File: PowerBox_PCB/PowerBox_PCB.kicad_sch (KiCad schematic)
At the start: 0 parts

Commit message: Added Powersupplys
Added the TPS54620 as powersupplys and built circuit for it.
Added A LDO 5v 3A DC-DC VREG for the battery charger
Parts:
- added R17: 10kΩ, Resistor_SMD:R_0805_2012Metric_Pad1.20x1.40mm_HandSolder, symbol Custom_Symbols:10kRes
- added U10: (no value), Package_TO_SOT_SMD:TO-252-3_TabPin2, symbol Batt_Charger:LM1084RS-5.0
- added U9: (no value), Package_TO_SOT_SMD:SOT-23, symbol Custom_Symbols:2N7002
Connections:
- new net GND: R17.2, U10.1 (GND), U9.2 (S)
- new net Ideal_Diode/VIN_IDEAL: R17.1, U9.1 (G)
- new net TPS54620_Buck1/EN_BUCK: U9.3 (D)
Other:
- added sheet Ideal_Diode (Ideal_Diode.kicad_sch)
- added sheet Ideal_Diode1 (Ideal_Diode.kicad_sch)
- added sheet TPS54620_Buck (TPS54620_Buck.kicad_sch)
- added sheet TPS54620_Buck1 (TPS54620_Buck.kicad_sch)

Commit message: Added USBPD & BMD & BATTCHARGER
Added USBPD & BMD & BATTCHARGER
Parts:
- removed U10: (no value), Package_TO_SOT_SMD:TO-252-3_TabPin2, symbol Batt_Charger:LM1084RS-5.0
- added B1: 2S Batt Pack, Custom_Footprints:2S Batt Pack, symbol Batt_Charger:BatteryPack
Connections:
- new net BMS/B+: B1.1 (B+)
- new net BMS/B-: B1.3 (B-)
- new net BMS/BM: B1.2 (BM)
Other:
- added sheet BMS (BMS.kicad_sch)
- added sheet Batt Charger (Batt Charger.kicad_sch)
- added sheet USBPD (USBPD.kicad_sch)

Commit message: Finished
Basically done
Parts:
- added SW1: SW_DPDT_x2, Custom_Footprints:SwitchPads, symbol BMS:SW_DPDT_x2
- added TP1, TP10, TP12, TP13, TP2, TP3, TP4, TP5, TP6, TP7, TP8, TP9: (no value), Custom_Footprints:PAD-2x2, symbol Custom_Symbols:Pad-2x2
- added TP14, TP15, TP16, TP17: (no value), Custom_Footprints:M3-Pad, symbol Custom_Symbols:M3-PAD
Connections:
- net GND: now also TP10.1 (PAD), TP14.1 (PAD), TP15.1 (PAD), TP16.1 (PAD), TP17.1 (PAD), TP2.1 (PAD), TP9.1 (PAD)
- net Ideal_Diode/VIN_IDEAL: now also TP13.1 (PAD)
- net Ideal_Diode/VOUT_IDEAL: now also TP6.1 (PAD), TP8.1 (PAD)
- net Ideal_Diode1/VIN_IDEAL: now also TP12.1 (PAD)
- net P+: now also SW1.5 (B), TP3.1 (PAD)
- net PM: now also TP4.1 (PAD)
- net VUSBPD: now also SW1.2 (B), TP1.1 (PAD)
- new net TPS54620_Buck1/VIN_BUCK: SW1.4 (A), TP5.1 (PAD)
- new net VUSBPDSWITCHED: SW1.1 (A), TP7.1 (PAD)

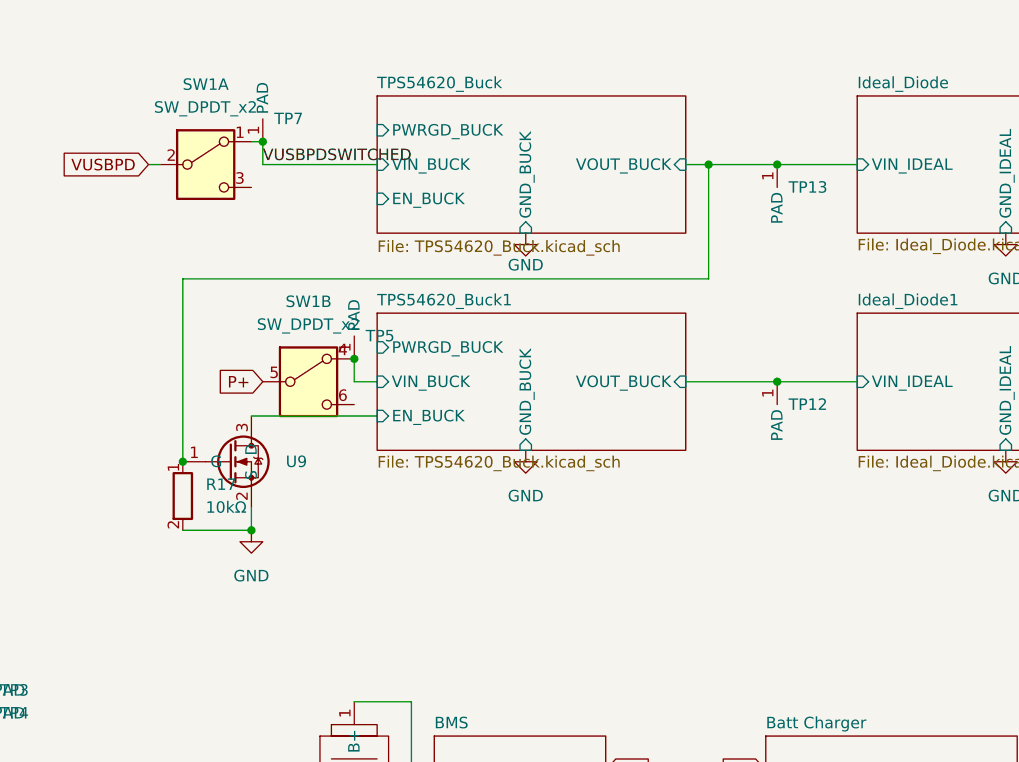
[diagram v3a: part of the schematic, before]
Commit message: add indicator lights
add indicator lights
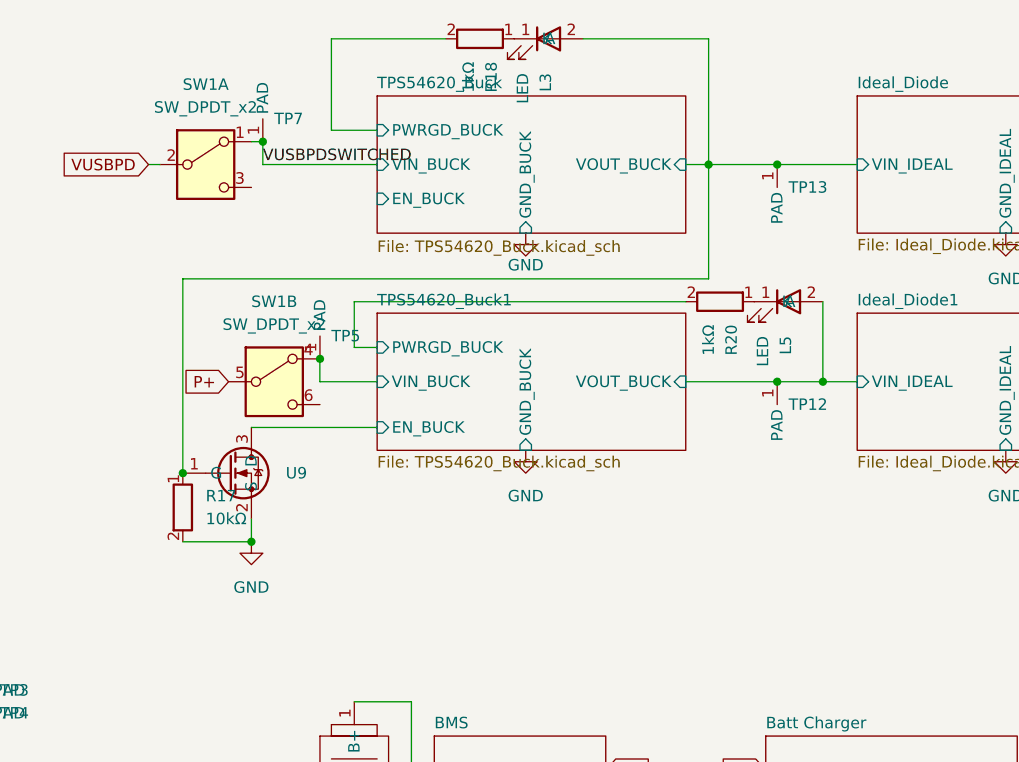
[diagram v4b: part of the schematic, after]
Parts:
- added L3, L5: LED, LED_SMD:LED_0805_2012Metric_Pad1.15x1.40mm_HandSolder, symbol Custom_Symbols:LED
- added R18, R20: 1kΩ, Resistor_SMD:R_0805_2012Metric_Pad1.20x1.40mm_HandSolder, symbol Custom_Symbols:1kRes
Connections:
- net Ideal_Diode/VIN_IDEAL: now also L3.2 (A)
- net Ideal_Diode1/VIN_IDEAL: now also L5.2 (A)
- net TPS54620_Buck/PWRGD_BUCK: now also R18.2
- net TPS54620_Buck1/PWRGD_BUCK: now also R20.2
- new net: L3.1 (K), R18.1
- new net: L5.1 (K), R20.1
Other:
- moved on the sheet: R17, SW1B, TP5, U9

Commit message: .
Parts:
- removed TP6, TP8: (no value), Custom_Footprints:PAD-2x2, symbol Custom_Symbols:Pad-2x2
- added TP18, TP19: (no value), Custom_Footprints:PAD-2x2-ThroughHole, symbol Custom_Symbols:Pad-2x2-ThroughHole
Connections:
- net Ideal_Diode/VOUT_IDEAL: now also TP18.1 (PAD), TP19.1 (PAD)

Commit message: fix bom
bom
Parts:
- U9: value (none) -> 2N7002
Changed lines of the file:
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@@
 			)
 		)
-		(property "Value" ""
+		(property "Value" "2N7002"
 			(at 127 81.28 0)
 			(show_name no)

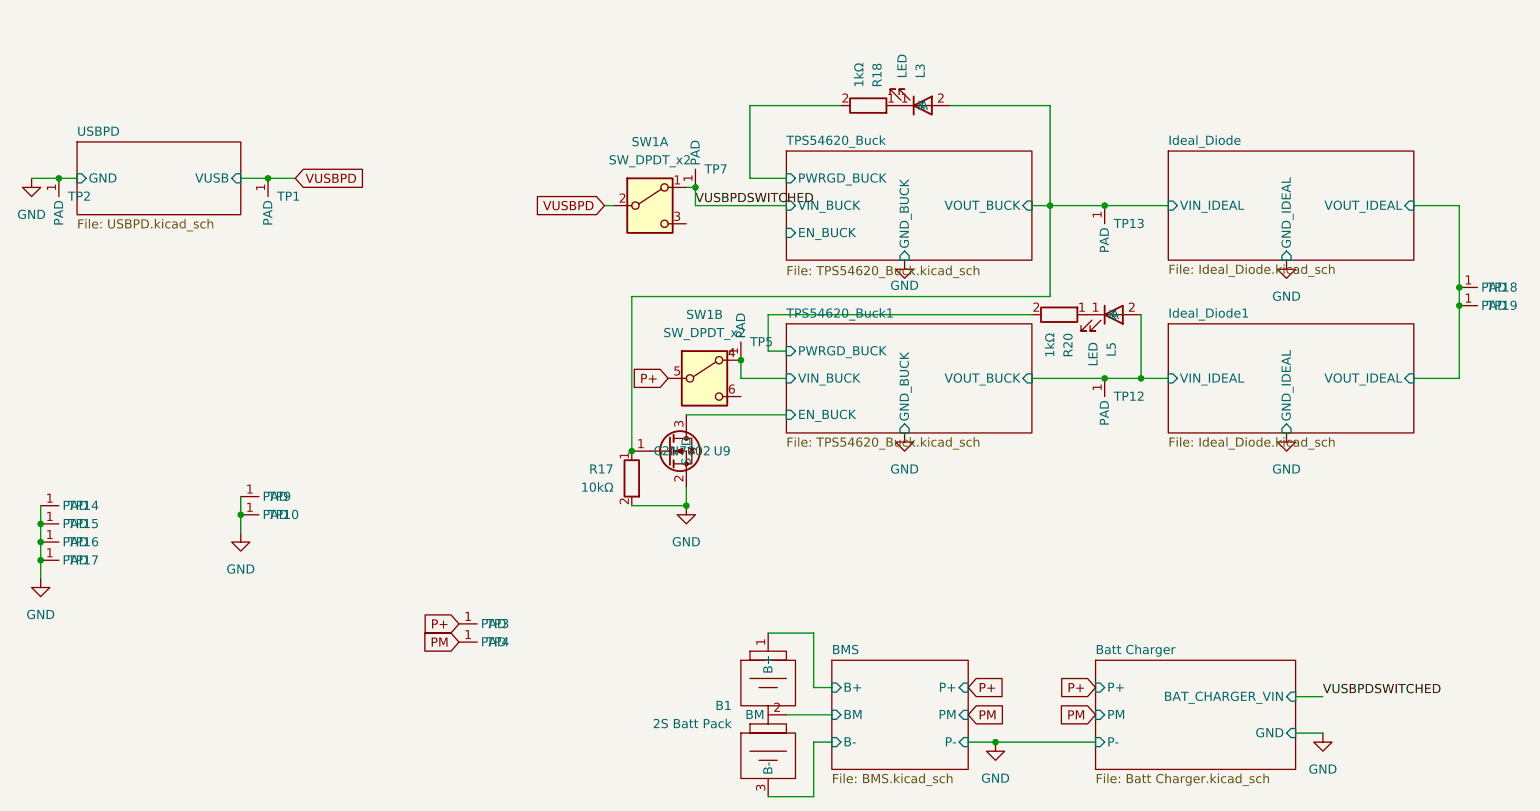
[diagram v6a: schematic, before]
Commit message: Changed HUSB238 to CH221K
HUSB238 Went out of stock so changed to CH221K
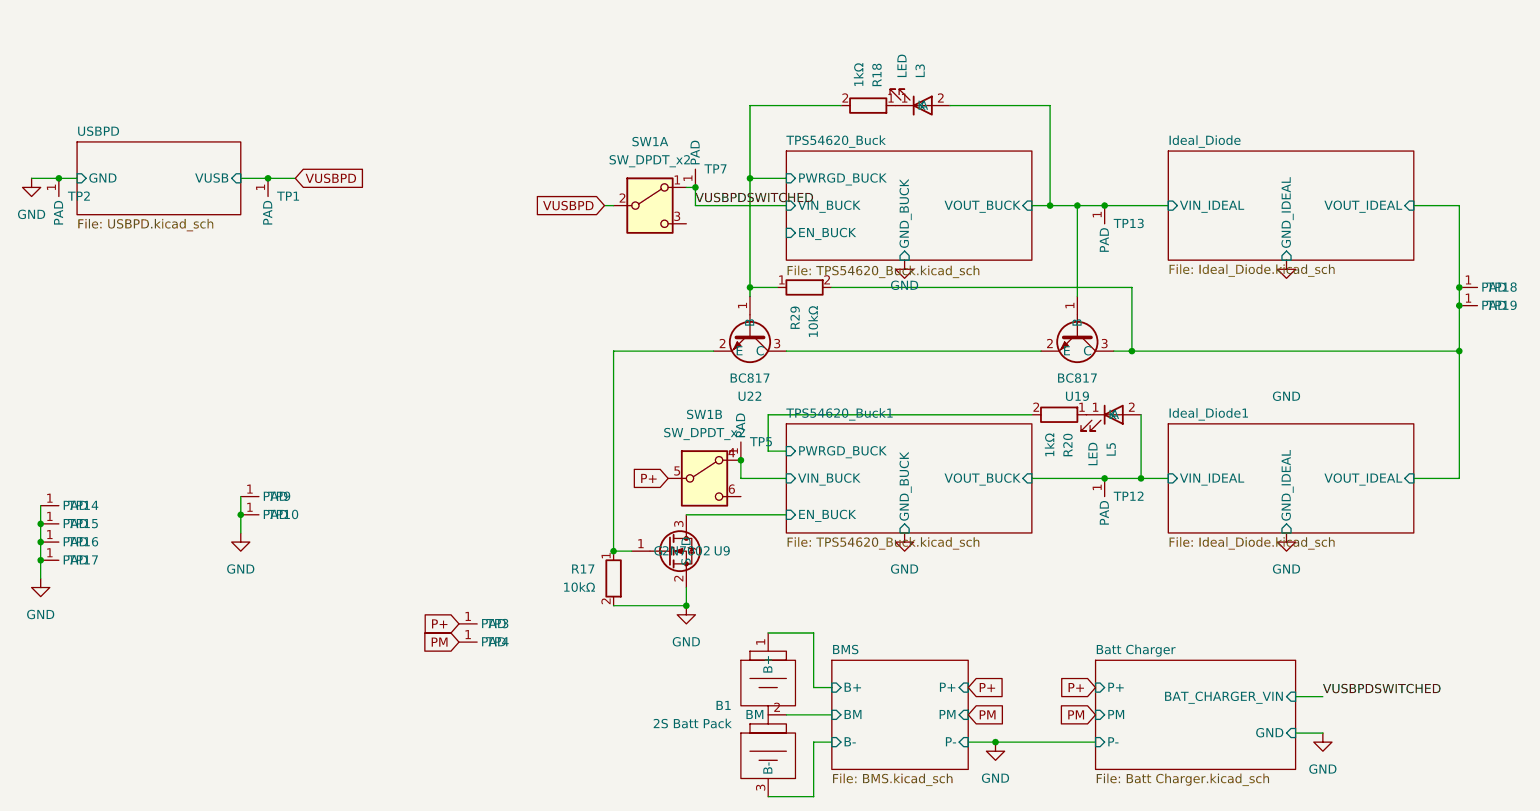
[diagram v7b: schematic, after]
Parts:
- added R29: 10kΩ, Resistor_SMD:R_0805_2012Metric_Pad1.20x1.40mm_HandSolder, symbol Custom_Symbols:10kRes
- added U19, U22: BC817, Package_TO_SOT_SMD:SOT-23, symbol Custom_Symbols:BC817-NPN
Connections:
- net Ideal_Diode/VIN_IDEAL: now also U19.1 (B); no longer R17.1, U9.1 (G)
- net Ideal_Diode/VOUT_IDEAL: now also R29.2, U19.3 (C)
- net TPS54620_Buck/PWRGD_BUCK: now also R29.1, U22.1 (B)
- new net: R17.1, U22.2 (E), U9.1 (G)
- new net: U19.2 (E), U22.3 (C)
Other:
- moved on the sheet: L5, R17, R20, SW1B, TP12, TP5, U9

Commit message: i finished and getting it made
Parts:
- removed R18, R20: 1kΩ, Resistor_SMD:R_0805_2012Metric_Pad1.20x1.40mm_HandSolder, symbol Custom_Symbols:1kRes
- added R26, R27: 2.2kΩ, Resistor_SMD:R_0805_2012Metric_Pad1.20x1.40mm_HandSolder, symbol Custom_Symbols:2.2kRes
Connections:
- net TPS54620_Buck/PWRGD_BUCK: now also R26.1
- net TPS54620_Buck1/PWRGD_BUCK: now also R27.1
- net at L3.1 (K): now also R26.2
- net at L5.1 (K): now also R27.2
- net Ideal_Diode/VIN_IDEAL renamed VUSBOUT
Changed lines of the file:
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@@
+	)
+	(junction
+		(at 189.23 46.99)
+		(diameter 0)
+		(color 0 0 0 0)
 	)
 	(junction
@@
 	(wire
 		(pts
+			(xy 189.23 46.99) (xy 194.31 46.99)
+		)
+		(stroke
+			(width 0)
+			(type default)
+		)
+	)
+	(wire
+		(pts
 			(xy 212.09 115.57) (xy 215.9 115.57)
 		)
@@
 	(wire
 		(pts
-			(xy 185.42 46.99) (xy 194.31 46.99)
+			(xy 185.42 46.99) (xy 189.23 46.99)
 		)
 		(stroke
@@
 	(wire
 		(pts
+			(xy 189.23 44.45) (xy 189.23 46.99)
+		)
+		(stroke
+			(width 0)
+			(type default)
+		)
+	)
+	(wire
+		(pts
 			(xy 135.89 43.18) (xy 135.89 58.42)
 		)
@@
 		)
 	)
-	(label "VUSBPDSWITCHED"
+	(label "VUSBOUT"
 		(at 215.9 115.57 0)
+		(effects
+			(font
+				(size 1.27 1.27)
+			)
+			(justify left bottom)
+		)
+	)
+	(label "VUSBOUT"
+		(at 189.23 44.45 90)
 		(effects
 			(font
@@
 	)
 	(symbol
-		(lib_id "Custom_Symbols:1kRes")
-		(at 152.4 33.02 270)
-		(mirror x)
-		(unit 1)
-		(body_style 1)
-		(exclude_from_sim no)
-		(in_bom yes)
-		(on_board yes)
-		(in_pos_files yes)
-		(dnp no)
-		(property "Reference" "R18"
-			(at 153.6701 30.48 0)
-			(show_name no)
-			(do_not_autoplace no)
-			(effects
-				(font
-					(size 1.27 1.27)
-				)
-				(justify left)
-			)
-		)
-		(property "Value" "1kΩ"
-			(at 151.1301 30.48 0)
-			(show_name no)
-			(do_not_autoplace no)
-			(effects
-				(font
-					(size 1.27 1.27)
-				)
-				(justify left)
-			)
-		)
-		(property "Footprint" "Resistor_SMD:R_0805_2012Metric_Pad1.20x1.40mm_HandSolder"
-			(at 152.4 33.02 0)
-			(hide yes)
-			(show_name no)
-			(do_not_autoplace no)
-			(effects
-				(font
-					(size 1.27 1.27)
-				)
-			)
-		)
-		(property "Datasheet" ""
-			(at 152.4 33.02 0)
-			(hide yes)
-			(show_name no)
-			(do_not_autoplace no)
-			(effects
-				(font
-					(size 1.27 1.27)
-				)
-			)
-		)
-		(property "Description" ""
-			(at 152.4 33.02 0)
-			(hide yes)
-			(show_name no)
-			(do_not_autoplace no)
-			(effects
-				(font
-					(size 1.27 1.27)
-				)
-			)
-		)
-		(pin "2"
-		)
-		(pin "1"
-		)
-		(instances
-			(project "PowerBox_PCB"
-				(path "/b0254e12-8cc0-427f-8cea-8f6ec8f66525"
-					(reference "R18")
-					(unit 1)
-				)
-			)
-		)
-	)
-	(symbol
 		(lib_id "power:GND")
 		(at 170.18 121.92 0)
@@
 				(path "/b0254e12-8cc0-427f-8cea-8f6ec8f66525"
 					(reference "#PWR022")
+					(unit 1)
+				)
+			)
+		)
+	)
+	(symbol
+		(lib_id "Custom_Symbols:2.2kRes")
+		(at 179.07 76.2 90)
+		(mirror x)
+		(unit 1)
+		(body_style 1)
+		(exclude_from_sim no)
+		(in_bom yes)
+		(on_board yes)
+		(in_pos_files yes)
+		(dnp no)
+		(property "Reference" "R27"
+			(at 179.07 82.55 90)
+			(show_name no)
+			(do_not_autoplace no)
+			(effects
+				(font
+					(size 1.27 1.27)
+				)
+			)
+		)
+		(property "Value" "2.2kΩ"
+			(at 179.07 80.01 90)
+			(show_name no)
+			(do_not_autoplace no)
+			(effects
+				(font
+					(size 1.27 1.27)
+				)
+			)
+		)
+		(property "Footprint" "Resistor_SMD:R_0805_2012Metric_Pad1.20x1.40mm_HandSolder"
+			(at 179.07 76.2 0)
+			(hide yes)
+			(show_name no)
+			(do_not_autoplace no)
+			(effects
+				(font
+					(size 1.27 1.27)
+				)
+			)
+		)
+		(property "Datasheet" ""
+			(at 179.07 76.2 0)
+			(hide yes)
+			(show_name no)
+			(do_not_autoplace no)
+			(effects
+				(font
+					(size 1.27 1.27)
+				)
+			)
+		)
+		(property "Description" ""
+			(at 179.07 76.2 0)
+			(hide yes)
+			(show_name no)
+			(do_not_autoplace no)
+			(effects
+				(font
+					(size 1.27 1.27)
+				)
+			)
+		)
+		(pin "2"
+		)
+		(pin "1"
+		)
+		(instances
+			(project "PowerBox_PCB"
+				(path "/b0254e12-8cc0-427f-8cea-8f6ec8f66525"
+					(reference "R27")
 					(unit 1)
 				)
@@
 	)
 	(symbol
-		(lib_id "Custom_Symbols:1kRes")
-		(at 179.07 76.2 270)
-		(unit 1)
-		(body_style 1)
-		(exclude_from_sim no)
-		(in_bom yes)
-		(on_board yes)
-		(in_pos_files yes)
-		(dnp no)
-		(fields_autoplaced yes)
-		(property "Reference" "R20"
-			(at 180.3401 78.74 0)
-			(show_name no)
-			(do_not_autoplace no)
-			(effects
-				(font
-					(size 1.27 1.27)
-				)
-				(justify left)
-			)
-		)
-		(property "Value" "1kΩ"
-			(at 177.8001 78.74 0)
-			(show_name no)
-			(do_not_autoplace no)
-			(effects
-				(font
-					(size 1.27 1.27)
-				)
-				(justify left)
-			)
-		)
-		(property "Footprint" "Resistor_SMD:R_0805_2012Metric_Pad1.20x1.40mm_HandSolder"
-			(at 179.07 76.2 0)
-			(hide yes)
-			(show_name no)
-			(do_not_autoplace no)
-			(effects
-				(font
-					(size 1.27 1.27)
-				)
-			)
-		)
-		(property "Datasheet" ""
-			(at 179.07 76.2 0)
-			(hide yes)
-			(show_name no)
-			(do_not_autoplace no)
-			(effects
-				(font
-					(size 1.27 1.27)
-				)
-			)
-		)
-		(property "Description" ""
-			(at 179.07 76.2 0)
-			(hide yes)
-			(show_name no)
-			(do_not_autoplace no)
-			(effects
-				(font
-					(size 1.27 1.27)
-				)
-			)
-		)
-		(pin "2"
-		)
-		(pin "1"
-		)
-		(instances
-			(project "PowerBox_PCB"
-				(path "/b0254e12-8cc0-427f-8cea-8f6ec8f66525"
-					(reference "R20")
-					(unit 1)
-				)
-			)
-		)
-	)
-	(symbol
 		(lib_id "Custom_Symbols:2N7002")
 		(at 127 95.25 0)
@@
 					(unit 1)
 				)
+			)
+		)
+	)
+	(symbol
+		(lib_id "Custom_Symbols:2.2kRes")
+		(at 152.4 33.02 90)
+		(unit 1)
+		(body_style 1)
+		(exclude_from_sim no)
+		(in_bom yes)
+		(on_board yes)
+		(in_pos_files yes)
+		(dnp no)
+		(property "Reference" "R26"
+			(at 152.4 26.67 90)
+			(show_name no)
+			(do_not_autoplace no)
+			(effects
+				(font
+					(size 1.27 1.27)
+				)
+			)
+		)
+		(property "Value" "2.2kΩ"
+			(at 152.4 29.21 90)
+			(show_name no)
+			(do_not_autoplace no)
+			(effects
+				(font
+					(size 1.27 1.27)
+				)
+			)
+		)
+		(property "Footprint" "Resistor_SMD:R_0805_2012Metric_Pad1.20x1.40mm_HandSolder"
+			(at 152.4 33.02 0)
+			(hide yes)
+			(show_name no)
+			(do_not_autoplace no)
+			(effects
+				(font
+					(size 1.27 1.27)
+				)
+			)
+		)
+		(property "Datasheet" ""
+			(at 152.4 33.02 0)
+			(hide yes)
+			(show_name no)
+			(do_not_autoplace no)
+			(effects
+				(font
+					(size 1.27 1.27)
+				)
+			)
+		)
+		(property "Description" ""
+			(at 152.4 33.02 0)
+			(hide yes)
+			(show_name no)
+			(do_not_autoplace no)
+			(effects
+				(font
+					(size 1.27 1.27)
+				)
+			)
+		)
+		(pin "2"
+		)
+		(pin "1"
+		)
+		(instances
+			(project "PowerBox_PCB"
+				(path "/b0254e12-8cc0-427f-8cea-8f6ec8f66525"
+					(reference "R26")
+					(unit 1)
+				)
